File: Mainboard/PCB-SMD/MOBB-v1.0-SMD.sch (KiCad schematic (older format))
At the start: 66 parts, among them P1 AUX 1-3, P14 EXTRA Pins, P2 Wire to Teensy VUSB, P3 +3.3V, P4 Pit Limiter, P5 Rotary Encoders, P6 BTN 1-32, P7 LED, Q1 NPN, Q2 NPN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

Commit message: * bit messy but the layout should work. still WIP
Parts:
- P1, P3: footprint Pin_Headers:Pin_Header_Angled_2x03 -> Socket_Strips:Socket_Strip_Angled_2x03
- P14: footprint Pin_Headers:Pin_Header_Angled_1x05 -> Socket_Strips:Socket_Strip_Angled_1x05
- P4: footprint Pin_Headers:Pin_Header_Angled_1x02 -> Socket_Strips:Socket_Strip_Angled_1x02
- P5: footprint Pin_Headers:Pin_Header_Angled_1x06 -> Socket_Strips:Socket_Strip_Angled_1x06
- P6: footprint Pin_Headers:Pin_Header_Angled_2x32 -> Socket_Strips:Socket_Strip_Angled_2x32
- P7: footprint Pin_Headers:Pin_Header_Straight_1x02 -> Socket_Strips:Socket_Strip_Straight_1x02
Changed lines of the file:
@@
 LIBS:resistor-star
 LIBS:Teensy3.2
+LIBS:MOBB-v1.0-SMD-cache
 EELAYER 25 0
 EELAYER END
@@
 F 0 "P5" H 9300 9250 50  0000 C CNN
 F 1 "Rotary Encoders" V 9400 8900 50  0000 C CNN
-F 2 "Pin_Headers:Pin_Header_Angled_1x06" H 9300 8900 50  0001 C CNN
+F 2 "Socket_Strips:Socket_Strip_Angled_1x06" H 9300 8900 50  0001 C CNN
 F 3 "" H 9300 8900 50  0000 C CNN
 	1    9300 8900
@@
 F 0 "P14" H 12500 9150 50  0000 C CNN
 F 1 "EXTRA Pins" V 12600 8850 50  0000 C CNN
-F 2 "Pin_Headers:Pin_Header_Angled_1x05" H 12500 8850 50  0001 C CNN
+F 2 "Socket_Strips:Socket_Strip_Angled_1x05" H 12500 8850 50  0001 C CNN
 F 3 "" H 12500 8850 50  0000 C CNN
 	1    12500 8850
@@
 F 0 "P1" H 7600 10650 50  0000 C CNN
 F 1 "AUX 1-3" H 7600 10250 50  0000 C CNN
-F 2 "Pin_Headers:Pin_Header_Angled_2x03" H 7600 9250 50  0001 C CNN
+F 2 "Socket_Strips:Socket_Strip_Angled_2x03" H 7600 9250 50  0001 C CNN
 F 3 "" H 7600 9250 50  0000 C CNN
 	1    7600 10450
@@
 F 0 "P3" H 13850 8000 50  0000 C CNN
 F 1 "+3.3V" H 13850 7600 50  0000 C CNN
-F 2 "Pin_Headers:Pin_Header_Angled_2x03" H 13850 6600 50  0001 C CNN
+F 2 "Socket_Strips:Socket_Strip_Angled_2x03" H 13850 6600 50  0001 C CNN
 F 3 "" H 13850 6600 50  0000 C CNN
 	1    13850 7800
@@
 F 0 "P6" H 10200 5100 50  0000 C CNN
 F 1 "BTN 1-32" V 10200 3450 50  0000 C CNN
-F 2 "Pin_Headers:Pin_Header_Angled_2x32" H 10200 3050 50  0001 C CNN
+F 2 "Socket_Strips:Socket_Strip_Angled_2x32" H 10200 3050 50  0001 C CNN
 F 3 "" H 10200 3050 50  0000 C CNN
 	1    10200 3450
@@
 F 0 "P4" H 9500 10650 50  0000 C CNN
 F 1 "Pit Limiter" V 9600 10500 50  0000 C CNN
-F 2 "Pin_Headers:Pin_Header_Angled_1x02" H 9500 10500 50  0001 C CNN
+F 2 "Socket_Strips:Socket_Strip_Angled_1x02" H 9500 10500 50  0001 C CNN
 F 3 "" H 9500 10500 50  0000 C CNN
 	1    9500 10500
@@
 F 0 "P7" H 11900 9800 50  0000 C CNN
 F 1 "LED" V 12000 9650 50  0000 C CNN
-F 2 "Pin_Headers:Pin_Header_Straight_1x02" H 11900 9650 50  0001 C CNN
+F 2 "Socket_Strips:Socket_Strip_Straight_1x02" H 11900 9650 50  0001 C CNN
 F 3 "" H 11900 9650 50  0000 C CNN
 	1    11900 9650

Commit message: * tweaked
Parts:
- C4: footprint Capacitors_ThroughHole:C_Disc_D3.0mm_W2.0mm_P2.50mm -> Capacitors_SMD:C_0805_HandSoldering
- P1, P3: footprint Socket_Strips:Socket_Strip_Angled_2x03 -> Pin_Headers:Pin_Header_Angled_2x03_Pitch2.54mm
- P14: footprint Socket_Strips:Socket_Strip_Angled_1x05 -> Pin_Headers:Pin_Header_Angled_1x05_Pitch2.54mm
- P2: footprint Socket_Strips:Socket_Strip_Straight_1x01 -> Pin_Headers:Pin_Header_Straight_1x01_Pitch2.54mm
- P4: footprint Socket_Strips:Socket_Strip_Angled_1x02 -> Pin_Headers:Pin_Header_Angled_1x02_Pitch2.54mm
- P5: footprint Socket_Strips:Socket_Strip_Angled_1x06 -> Pin_Headers:Pin_Header_Angled_1x06_Pitch2.54mm
- P6: footprint Socket_Strips:Socket_Strip_Angled_2x32 -> Pin_Headers:Pin_Header_Angled_2x32_Pitch2.54mm
- P7: footprint Socket_Strips:Socket_Strip_Straight_1x02 -> Pin_Headers:Pin_Header_Angled_1x02_Pitch2.54mm
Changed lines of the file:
@@
 F 0 "P5" H 9300 9250 50  0000 C CNN
 F 1 "Rotary Encoders" V 9400 8900 50  0000 C CNN
-F 2 "Socket_Strips:Socket_Strip_Angled_1x06" H 9300 8900 50  0001 C CNN
+F 2 "Pin_Headers:Pin_Header_Angled_1x06_Pitch2.54mm" H 9300 8900 50  0001 C CNN
 F 3 "" H 9300 8900 50  0000 C CNN
 	1    9300 8900
@@
 F 0 "P14" H 12500 9150 50  0000 C CNN
 F 1 "EXTRA Pins" V 12600 8850 50  0000 C CNN
-F 2 "Socket_Strips:Socket_Strip_Angled_1x05" H 12500 8850 50  0001 C CNN
+F 2 "Pin_Headers:Pin_Header_Angled_1x05_Pitch2.54mm" H 12500 8850 50  0001 C CNN
 F 3 "" H 12500 8850 50  0000 C CNN
 	1    12500 8850
@@
 F 0 "P1" H 7600 10650 50  0000 C CNN
 F 1 "AUX 1-3" H 7600 10250 50  0000 C CNN
-F 2 "Socket_Strips:Socket_Strip_Angled_2x03" H 7600 9250 50  0001 C CNN
+F 2 "Pin_Headers:Pin_Header_Angled_2x03_Pitch2.54mm" H 7600 9250 50  0001 C CNN
 F 3 "" H 7600 9250 50  0000 C CNN
 	1    7600 10450
@@
 F 0 "P2" H 10350 10450 50  0000 C CNN
 F 1 "Wire to Teensy VUSB" V 10450 10350 50  0000 C CNN
-F 2 "Socket_Strips:Socket_Strip_Straight_1x01" H 10350 10350 50  0001 C CNN
+F 2 "Pin_Headers:Pin_Header_Straight_1x01_Pitch2.54mm" H 10350 10350 50  0001 C CNN
 F 3 "" H 10350 10350 50  0000 C CNN
 	1    10350 10350
@@
 F 0 "P3" H 13850 8000 50  0000 C CNN
 F 1 "+3.3V" H 13850 7600 50  0000 C CNN
-F 2 "Socket_Strips:Socket_Strip_Angled_2x03" H 13850 6600 50  0001 C CNN
+F 2 "Pin_Headers:Pin_Header_Angled_2x03_Pitch2.54mm" H 13850 6600 50  0001 C CNN
 F 3 "" H 13850 6600 50  0000 C CNN
 	1    13850 7800
@@
 F 0 "P6" H 10200 5100 50  0000 C CNN
 F 1 "BTN 1-32" V 10200 3450 50  0000 C CNN
-F 2 "Socket_Strips:Socket_Strip_Angled_2x32" H 10200 3050 50  0001 C CNN
+F 2 "Pin_Headers:Pin_Header_Angled_2x32_Pitch2.54mm" H 10200 3050 50  0001 C CNN
 F 3 "" H 10200 3050 50  0000 C CNN
 	1    10200 3450
@@
 F 0 "P4" H 9500 10650 50  0000 C CNN
 F 1 "Pit Limiter" V 9600 10500 50  0000 C CNN
-F 2 "Socket_Strips:Socket_Strip_Angled_1x02" H 9500 10500 50  0001 C CNN
+F 2 "Pin_Headers:Pin_Header_Angled_1x02_Pitch2.54mm" H 9500 10500 50  0001 C CNN
 F 3 "" H 9500 10500 50  0000 C CNN
 	1    9500 10500
@@
 F 0 "C4" H 12325 7900 50  0000 L CNN
 F 1 "C" H 12325 7700 50  0000 L CNN
-F 2 "Capacitors_ThroughHole:C_Disc_D3.0mm_W2.0mm_P2.50mm" H 12338 7650 50  0001 C CNN
+F 2 "Capacitors_SMD:C_0805_HandSoldering" H 12338 7650 50  0001 C CNN
 F 3 "" H 12300 7800 50  0000 C CNN
 	1    12300 7800
@@
 F 0 "P7" H 11900 9800 50  0000 C CNN
 F 1 "LED" V 12000 9650 50  0000 C CNN
-F 2 "Socket_Strips:Socket_Strip_Straight_1x02" H 11900 9650 50  0001 C CNN
+F 2 "Pin_Headers:Pin_Header_Angled_1x02_Pitch2.54mm" H 11900 9650 50  0001 C CNN
 F 3 "" H 11900 9650 50  0000 C CNN
 	1    11900 9650

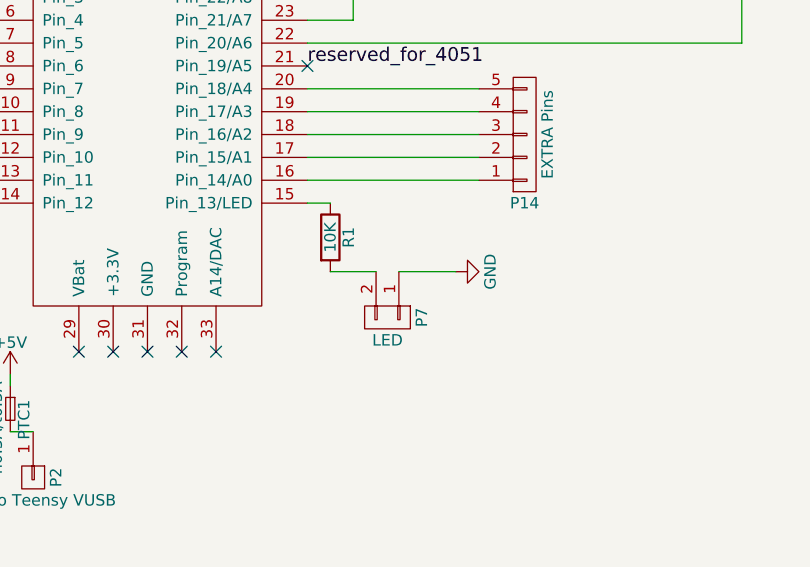
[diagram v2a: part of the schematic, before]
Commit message: * added bottom mounting hole and ground connections
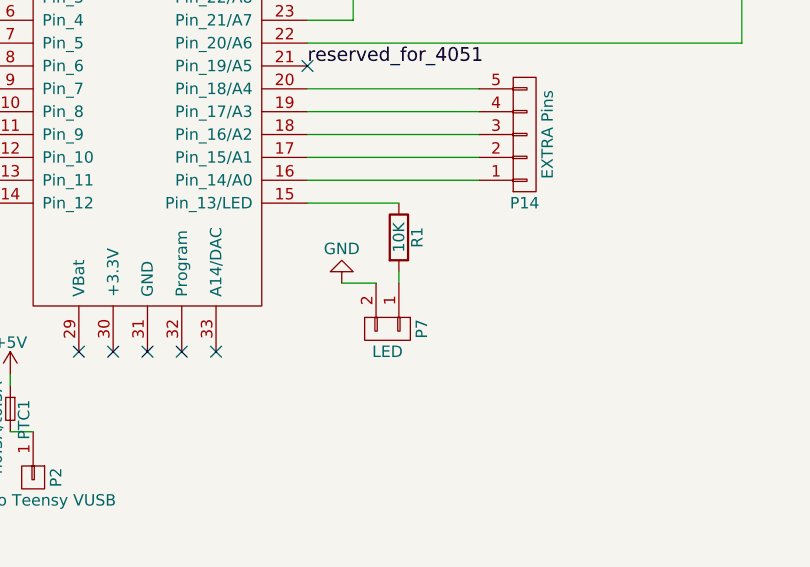
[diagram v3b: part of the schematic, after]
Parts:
- C7: footprint Capacitors_SMD:C_0805_HandSoldering -> Capacitors_ThroughHole:CP_Radial_D6.3mm_P2.50mm
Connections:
- net GND: now also P7.2 (P2); no longer P7.1 (P1)
- net at R1.2: now also P7.1 (P1); no longer P7.2 (P2)
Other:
- moved on the sheet: P7, R1
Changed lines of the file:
@@
 F 0 "C7" H 12525 7900 50  0000 L CNN
 F 1 "CP" H 12525 7700 50  0000 L CNN
-F 2 "Capacitors_SMD:C_0805_HandSoldering" H 12538 7650 50  0001 C CNN
+F 2 "Capacitors_ThroughHole:CP_Radial_D6.3mm_P2.50mm" H 12538 7650 50  0001 C CNN
 F 3 "" H 12500 7800 50  0000 C CNN
 	1    12500 7800
@@
 L R R1
 U 1 1 584D5813
-P 11650 9300
-F 0 "R1" V 11730 9300 50  0000 C CNN
-F 1 "10K" V 11650 9300 50  0000 C CNN
-F 2 "Resistors_SMD:R_0805_HandSoldering" V 11580 9300 50  0001 C CNN
-F 3 "" H 11650 9300 50  0000 C CNN
-	1    11650 9300
+P 11950 9300
+F 0 "R1" V 12030 9300 50  0000 C CNN
+F 1 "10K" V 11950 9300 50  0000 C CNN
+F 2 "Resistors_SMD:R_0805_HandSoldering" V 11880 9300 50  0001 C CNN
+F 3 "" H 11950 9300 50  0000 C CNN
+	1    11950 9300
 	1    0    0    -1
 $EndComp
@@
 L GND #PWR024
 U 1 1 584D5949
-P 12200 9450
-F 0 "#PWR024" H 12200 9200 50  0001 C CNN
-F 1 "GND" H 12200 9300 50  0000 C CNN
-F 2 "" H 12200 9450 50  0000 C CNN
-F 3 "" H 12200 9450 50  0000 C CNN
-	1    12200 9450
-	0    -1   -1   0
-$EndComp
-Wire Wire Line
-	11550 9150 11650 9150
-Wire Wire Line
-	11650 9450 11850 9450
-Wire Wire Line
-	11950 9450 12200 9450
+P 11700 9500
+F 0 "#PWR024" H 11700 9250 50  0001 C CNN
+F 1 "GND" H 11700 9350 50  0000 C CNN
+F 2 "" H 11700 9500 50  0000 C CNN
+F 3 "" H 11700 9500 50  0000 C CNN
+	1    11700 9500
+	-1   0    0    1
+$EndComp
+Wire Wire Line
+	11550 9150 11950 9150
 $Comp
 L CONN_01X02 P7
 U 1 1 584D6310
-P 11900 9650
-F 0 "P7" H 11900 9800 50  0000 C CNN
-F 1 "LED" V 12000 9650 50  0000 C CNN
-F 2 "Pin_Headers:Pin_Header_Angled_1x02_Pitch2.54mm" H 11900 9650 50  0001 C CNN
-F 3 "" H 11900 9650 50  0000 C CNN
-	1    11900 9650
+P 11900 9700
+F 0 "P7" H 11900 9850 50  0000 C CNN
+F 1 "LED" V 12000 9700 50  0000 C CNN
+F 2 "Pin_Headers:Pin_Header_Angled_1x02_Pitch2.54mm" H 11900 9700 50  0001 C CNN
+F 3 "" H 11900 9700 50  0000 C CNN
+	1    11900 9700
 	0    1    1    0
 $EndComp
@@
 Wire Wire Line
 	7950 7600 7850 7600
+Wire Wire Line
+	11850 9500 11700 9500
+Wire Wire Line
+	11950 9500 11950 9450
 $EndSCHEMATC
